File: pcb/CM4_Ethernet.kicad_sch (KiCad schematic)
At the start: 17 parts, among them U1 74LVC1G07SE-7, U1 TPD4EUSB30, U2 TPD4EUSB30, U3 MagJack-A70-112-331N126

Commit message: - voor aanpassing design rules jclpcb
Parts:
- D1, D2: footprint LED_SMD:LED_0603_1608Metric -> LED_SMD:LED_0805_2012Metric_Pad1.15x1.40mm_HandSolder
- R1, R2, R3: footprint Resistor_SMD:R_0402_1005Metric -> Resistor_SMD:R_0805_2012Metric_Pad1.20x1.40mm_HandSolder
- TP1, TP2: footprint TestPoint:TestPoint_Pad_2.0x2.0mm -> TestPoint:TestPoint_Bridge_Pitch2.54mm_Drill1.0mm
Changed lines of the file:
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@@
       (effects (font (size 1.27 1.27)) (justify left))
     )
-    (property "Footprint" "Resistor_SMD:R_0402_1005Metric" (at 128.016 48.26 90)
+    (property "Footprint" "Resistor_SMD:R_0805_2012Metric_Pad1.20x1.40mm_HandSolder" (at 128.016 48.26 90)
       (effects (font (size 1.27 1.27)) hide)
     )
@@
       (effects (font (size 1.27 1.27)) (justify right))
     )
-    (property "Footprint" "LED_SMD:LED_0603_1608Metric" (at 165.1 129.54 0)
+    (property "Footprint" "LED_SMD:LED_0805_2012Metric_Pad1.15x1.40mm_HandSolder" (at 165.1 129.54 0)
       (effects (font (size 1.27 1.27)) hide)
     )
@@
       (effects (font (size 1.27 1.27)))
     )
-    (property "Footprint" "Resistor_SMD:R_0402_1005Metric" (at 215.9 88.392 90)
+    (property "Footprint" "Resistor_SMD:R_0805_2012Metric_Pad1.20x1.40mm_HandSolder" (at 215.9 88.392 90)
       (effects (font (size 1.27 1.27)) hide)
     )
@@
       (effects (font (size 1.27 1.27)) (justify left))
     )
-    (property "Footprint" "TestPoint:TestPoint_Pad_2.0x2.0mm" (at 160.0962 128.397 0)
+    (property "Footprint" "TestPoint:TestPoint_Bridge_Pitch2.54mm_Drill1.0mm" (at 160.0962 128.397 0)
       (effects (font (size 1.27 1.27)) hide)
     )
@@
       (effects (font (size 1.27 1.27)) (justify right))
     )
-    (property "Footprint" "LED_SMD:LED_0603_1608Metric" (at 129.794 35.56 0)
+    (property "Footprint" "LED_SMD:LED_0805_2012Metric_Pad1.15x1.40mm_HandSolder" (at 129.794 35.56 0)
       (effects (font (size 1.27 1.27)) hide)
     )
@@
       (effects (font (size 1.27 1.27)) (justify left))
     )
-    (property "Footprint" "TestPoint:TestPoint_Pad_2.0x2.0mm" (at 136.144 46.99 0)
+    (property "Footprint" "TestPoint:TestPoint_Bridge_Pitch2.54mm_Drill1.0mm" (at 136.144 46.99 0)
       (effects (font (size 1.27 1.27)) hide)
     )
@@
       (effects (font (size 1.27 1.27)))
     )
-    (property "Footprint" "Resistor_SMD:R_0402_1005Metric" (at 215.9 83.312 90)
+    (property "Footprint" "Resistor_SMD:R_0805_2012Metric_Pad1.20x1.40mm_HandSolder" (at 215.9 83.312 90)
       (effects (font (size 1.27 1.27)) hide)
     )
@@
       (effects (font (size 1.27 1.27)) (justify left))
     )
-    (property "Footprint" "Resistor_SMD:R_0402_1005Metric" (at 163.322 138.43 90)
-      (effects (font (size 1.27 1.27)) hide)
-    )
+    (property "Footprint" "Resistor_SMD:R_0805_2012Metric_Pad1.20x1.40mm_HandSolder" (at 163.322 138.43 90)
+      (effects (font (size 1.27 1.27)) hide)
+    )

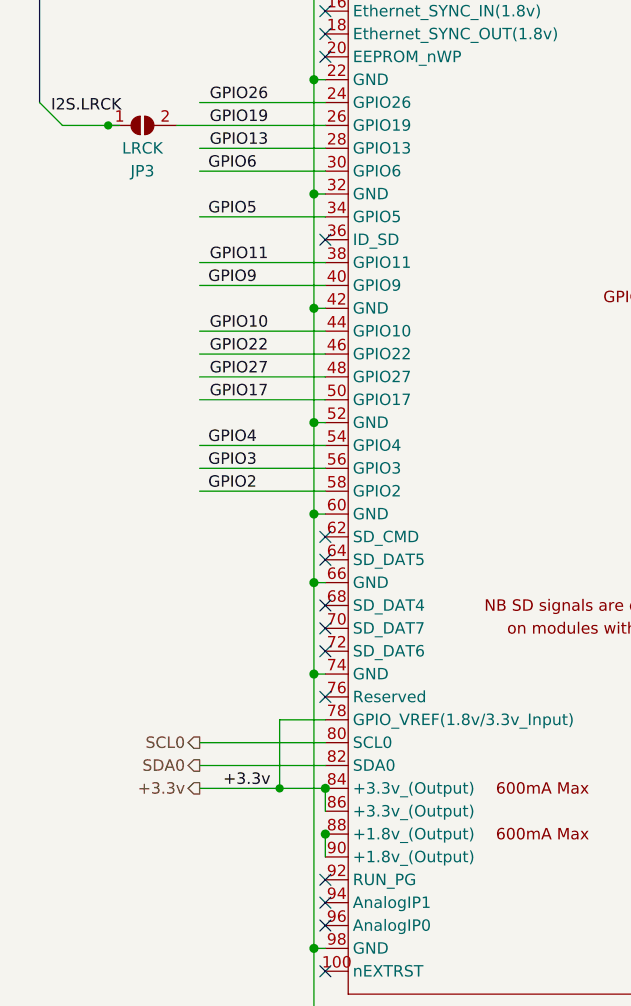
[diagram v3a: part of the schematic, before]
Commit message: - amp connected
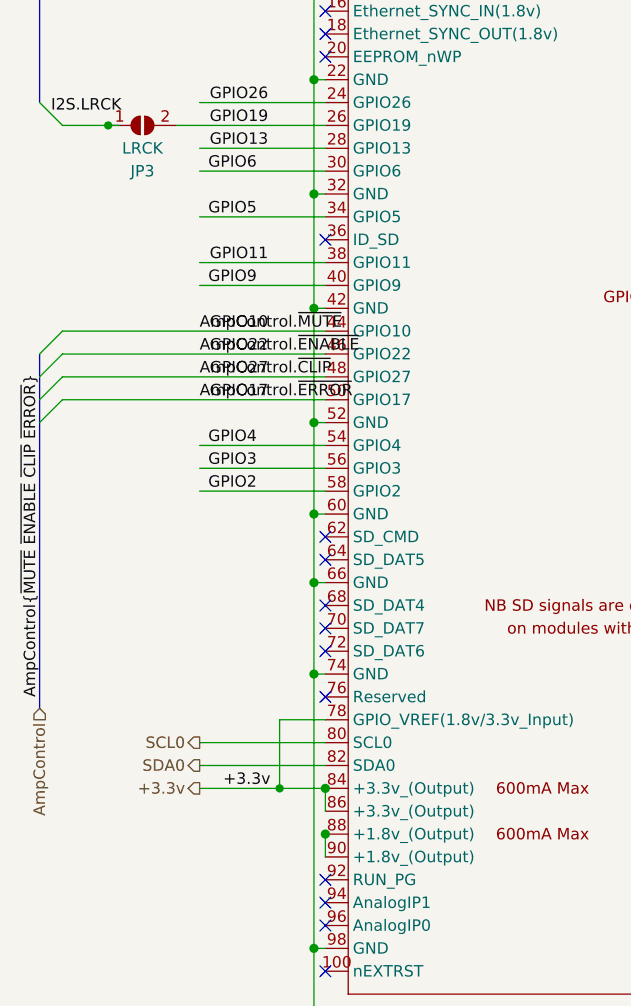
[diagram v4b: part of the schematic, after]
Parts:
- JP3: footprint (none) -> Jumper:SolderJumper-2_P1.3mm_Open_TrianglePad1.0x1.5mm
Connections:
- net GPIO10 renamed AmpControl.~{MUTE}
- net GPIO17 renamed AmpControl.~{ERROR}
- net GPIO22 renamed AmpControl.~{ENABLE}
- net GPIO27 renamed AmpControl.~{CLIP}
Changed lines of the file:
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@@
+    (stroke (width 0) (type default))
+  )
+  (bus_entry (at 20.32 90.17) (size 2.54 -2.54)
     (stroke (width 0) (type default))
   )
@@
     (stroke (width 0) (type default))
   )
+  (bus_entry (at 20.32 87.63) (size 2.54 -2.54)
+    (stroke (width 0) (type default))
+  )
+  (bus_entry (at 20.32 92.71) (size 2.54 -2.54)
+    (stroke (width 0) (type default))
+  )
+  (bus_entry (at 20.32 85.09) (size 2.54 -2.54)
+    (stroke (width 0) (type default))
+  )
   (bus_entry (at 144.78 87.63) (size -2.54 2.54)
     (stroke (width 0) (type default))
@@
     (stroke (width 0) (type solid))
   )
+  (bus (pts (xy 20.32 90.17) (xy 20.32 92.71))
+    (stroke (width 0) (type default))
+  )
   (wire (pts (xy 168.91 38.1) (xy 177.8 38.1))
     (stroke (width 0) (type solid))
@@
     (stroke (width 0) (type solid))
   )
+  (wire (pts (xy 22.86 85.09) (xy 52.07 85.09))
+    (stroke (width 0) (type default))
+  )
   (wire (pts (xy 113.03 80.01) (xy 127 80.01))
     (stroke (width 0) (type solid))
@@
     (stroke (width 0) (type solid))
   )
+  (bus (pts (xy 20.32 85.09) (xy 20.32 87.63))
+    (stroke (width 0) (type default))
+  )
   (wire (pts (xy 229.87 97.79) (xy 229.87 100.33))
     (stroke (width 0) (type solid))
@@
     (stroke (width 0) (type solid))
   )
-  (wire (pts (xy 38.1 90.17) (xy 52.07 90.17))
+  (wire (pts (xy 22.86 90.17) (xy 52.07 90.17))
     (stroke (width 0) (type solid))
   )
@@
     (stroke (width 0) (type default))
   )
+  (wire (pts (xy 22.86 82.55) (xy 52.07 82.55))
+    (stroke (width 0) (type default))
+  )
   (wire (pts (xy 113.03 41.91) (xy 125.984 41.91))
     (stroke (width 0) (type solid))
@@
     (stroke (width 0) (type solid))
   )
+  (bus (pts (xy 20.32 92.71) (xy 20.32 124.46))
+    (stroke (width 0) (type default))
+  )
   (wire (pts (xy 35.56 59.69) (xy 52.07 59.69))
     (stroke (width 0) (type default))
@@
     (stroke (width 0) (type default))
   )
-  (wire (pts (xy 38.1 82.55) (xy 52.07 82.55))
-    (stroke (width 0) (type solid))
-  )
-  (wire (pts (xy 38.1 85.09) (xy 52.07 85.09))
-    (stroke (width 0) (type solid))
-  )
   (wire (pts (xy 113.03 133.35) (xy 113.03 135.89))
     (stroke (width 0) (type solid))
@@
     (stroke (width 0) (type solid))
   )
-  (wire (pts (xy 38.1 87.63) (xy 52.07 87.63))
+  (wire (pts (xy 22.86 87.63) (xy 52.07 87.63))
     (stroke (width 0) (type solid))
   )
@@
   )
   (wire (pts (xy 22.86 59.69) (xy 27.94 59.69))
+    (stroke (width 0) (type default))
+  )
+  (bus (pts (xy 20.32 87.63) (xy 20.32 90.17))
     (stroke (width 0) (type default))
   )
@@
     (effects (font (size 1.27 1.27)) (justify right bottom))
   )
+  (label "AmpControl.~{MUTE}" (at 38.1 82.55 0)
+    (effects (font (size 1.27 1.27)) (justify left bottom))
+  )
+  (label "AmpControl.~{ERROR}" (at 38.1 90.17 0)
+    (effects (font (size 1.27 1.27)) (justify left bottom))
+  )
   (label "TRD3_N" (at 176.53 43.18 180) (fields_autoplaced)
     (effects (font (size 1.27 1.27)) (justify right bottom))
@@
     (effects (font (size 1.27 1.27)) (justify right bottom))
   )
+  (label "AmpControl.~{ENABLE}" (at 38.1 85.09 0)
+    (effects (font (size 1.27 1.27)) (justify left bottom))
+  )
   (label "TRD3_P" (at 115.824 31.75 0) (fields_autoplaced)
     (effects (font (size 1.27 1.27)) (justify left bottom))
@@
     (effects (font (size 1.27 1.27)) (justify right bottom))
   )
+  (label "AmpControl{~{MUTE} ~{ENABLE} ~{CLIP} ~{ERROR}}" (at 20.32 123.19 90) (fields_autoplaced)
+    (effects (font (size 1.27 1.27)) (justify left bottom))
+  )
   (label "TRD1_P" (at 228.6 39.37 180) (fields_autoplaced)
     (effects (font (size 1.27 1.27)) (justify right bottom))
@@
   )
   (label "I2S.D" (at 137.16 59.69 0)
+    (effects (font (size 1.27 1.27)) (justify left bottom))
+  )
+  (label "AmpControl.~{CLIP}" (at 38.1 87.63 0)
     (effects (font (size 1.27 1.27)) (justify left bottom))
   )
@@
     (effects (font (size 1.27 1.27)) (justify right))
   )
+  (hierarchical_label "AmpControl" (shape input) (at 20.32 124.46 270) (fields_autoplaced)
+    (effects (font (size 1.27 1.27)) (justify right))
+  )
   (hierarchical_label "SDA0" (shape output) (at 38.1 130.81 180) (fields_autoplaced)
     (effects (font (size 1.27 1.27)) (justify right))
@@
       (effects (font (size 1.27 1.27)))
     )
-    (property "Footprint" "" (at 31.75 59.69 0)
+    (property "Footprint" "Jumper:SolderJumper-2_P1.3mm_Open_TrianglePad1.0x1.5mm" (at 31.75 59.69 0)
       (effects (font (size 1.27 1.27)) hide)
     )
@@
       (effects (font (size 1.27 1.27)))
     )
-    (property "Footprint" "" (at 134.62 59.69 0)
+    (property "Footprint" "Jumper:SolderJumper-2_P1.3mm_Open_TrianglePad1.0x1.5mm" (at 134.62 59.69 0)
       (effects (font (size 1.27 1.27)) hide)
     )
@@
       (effects (font (size 1.27 1.27)))
     )
-    (property "Footprint" "" (at 134.62 90.17 0)
-      (effects (font (size 1.27 1.27)) hide)
-    )
+    (property "Footprint" "Jumper:SolderJumper-2_P1.3mm_Open_TrianglePad1.0x1.5mm" (at 134.62 90.17 0)
+      (effects (font (size 1.27 1.27)) hide)
+    )

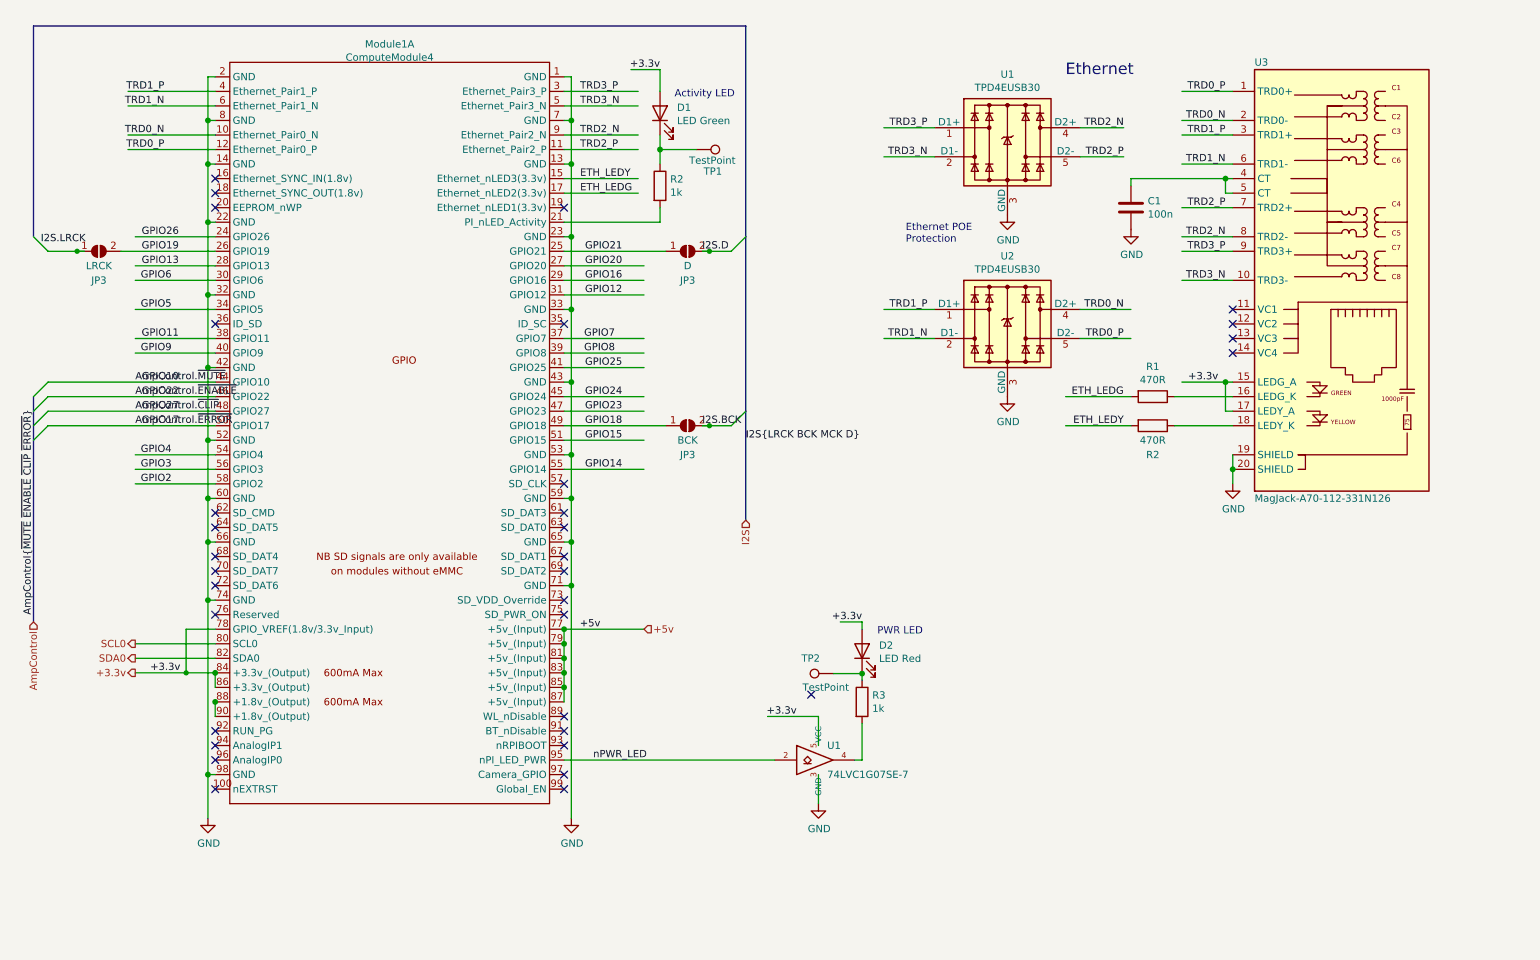
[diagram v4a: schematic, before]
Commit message: - cleanup ERC errors
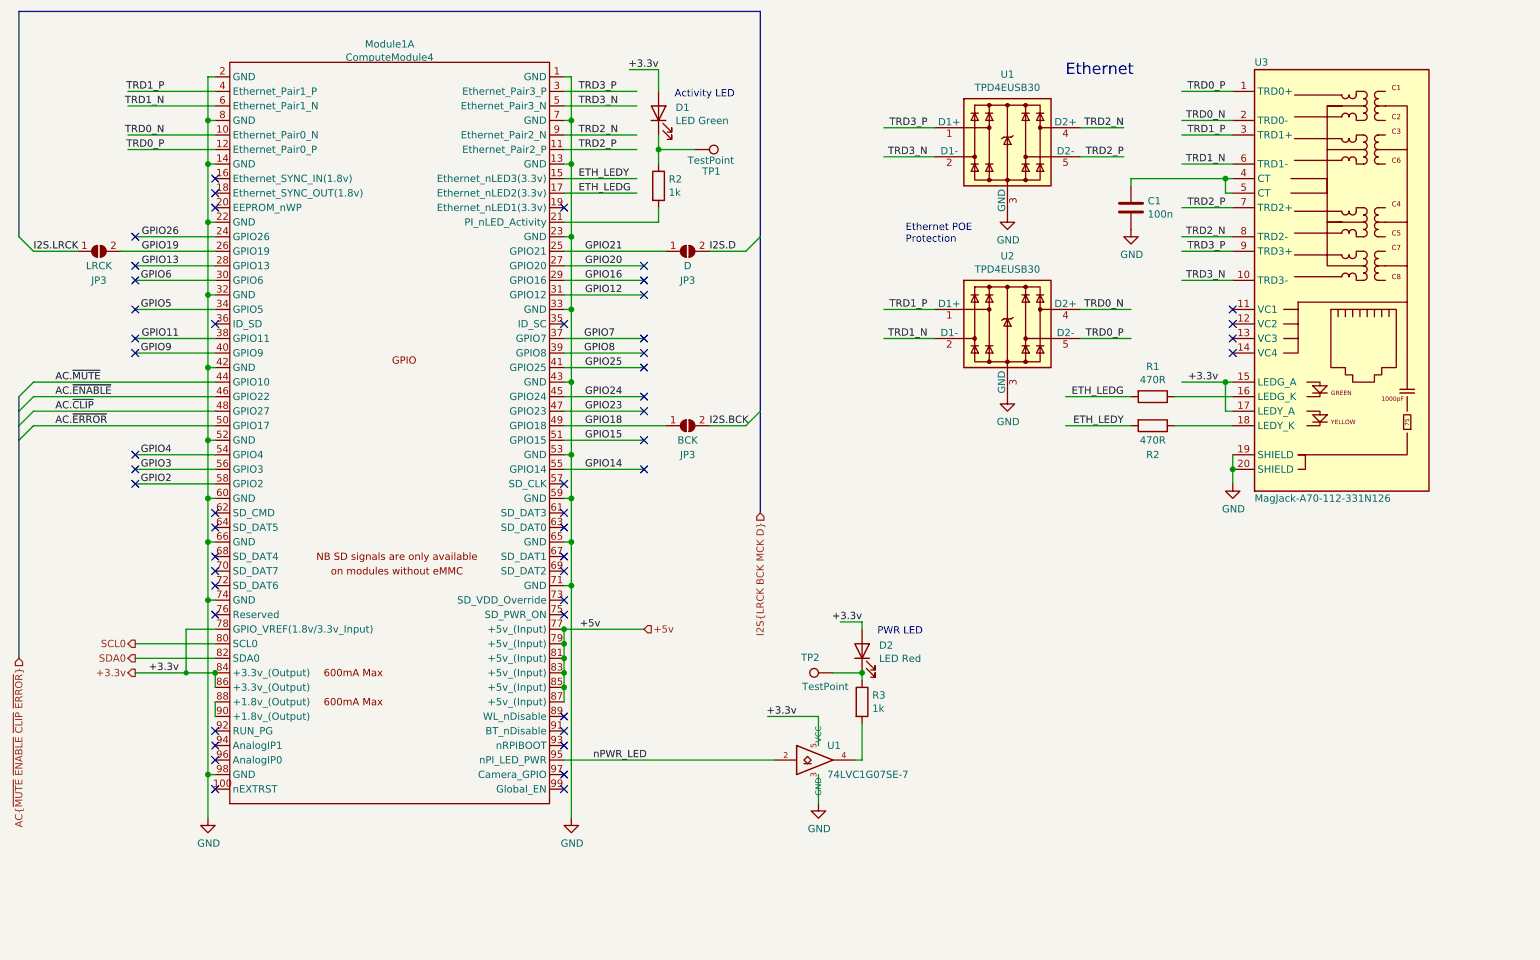
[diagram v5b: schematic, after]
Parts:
- Module1: footprint CM4IO:Raspberry-Pi-4-Compute-Module -> Footprints:Raspberry-Pi-4-Compute-Module
- U3: footprint CM4IO:TRJG0926HENL -> Footprints:TRJG0926HENL
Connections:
- net I2S.LRCK: now also JP3.1 (A)
- net AmpControl.~{CLIP} renamed AC.~{CLIP}
- net AmpControl.~{ENABLE} renamed AC.~{ENABLE}
- net AmpControl.~{ERROR} renamed AC.~{ERROR}
- net AmpControl.~{MUTE} renamed AC.~{MUTE}
- no-connect marks 33 -> 51
